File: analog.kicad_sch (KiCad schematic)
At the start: 50 parts, among them J10 Spare diff in, J9 Sensor harness, U8 ADS1115 (0x48), U9 ADS1115 (0x49)

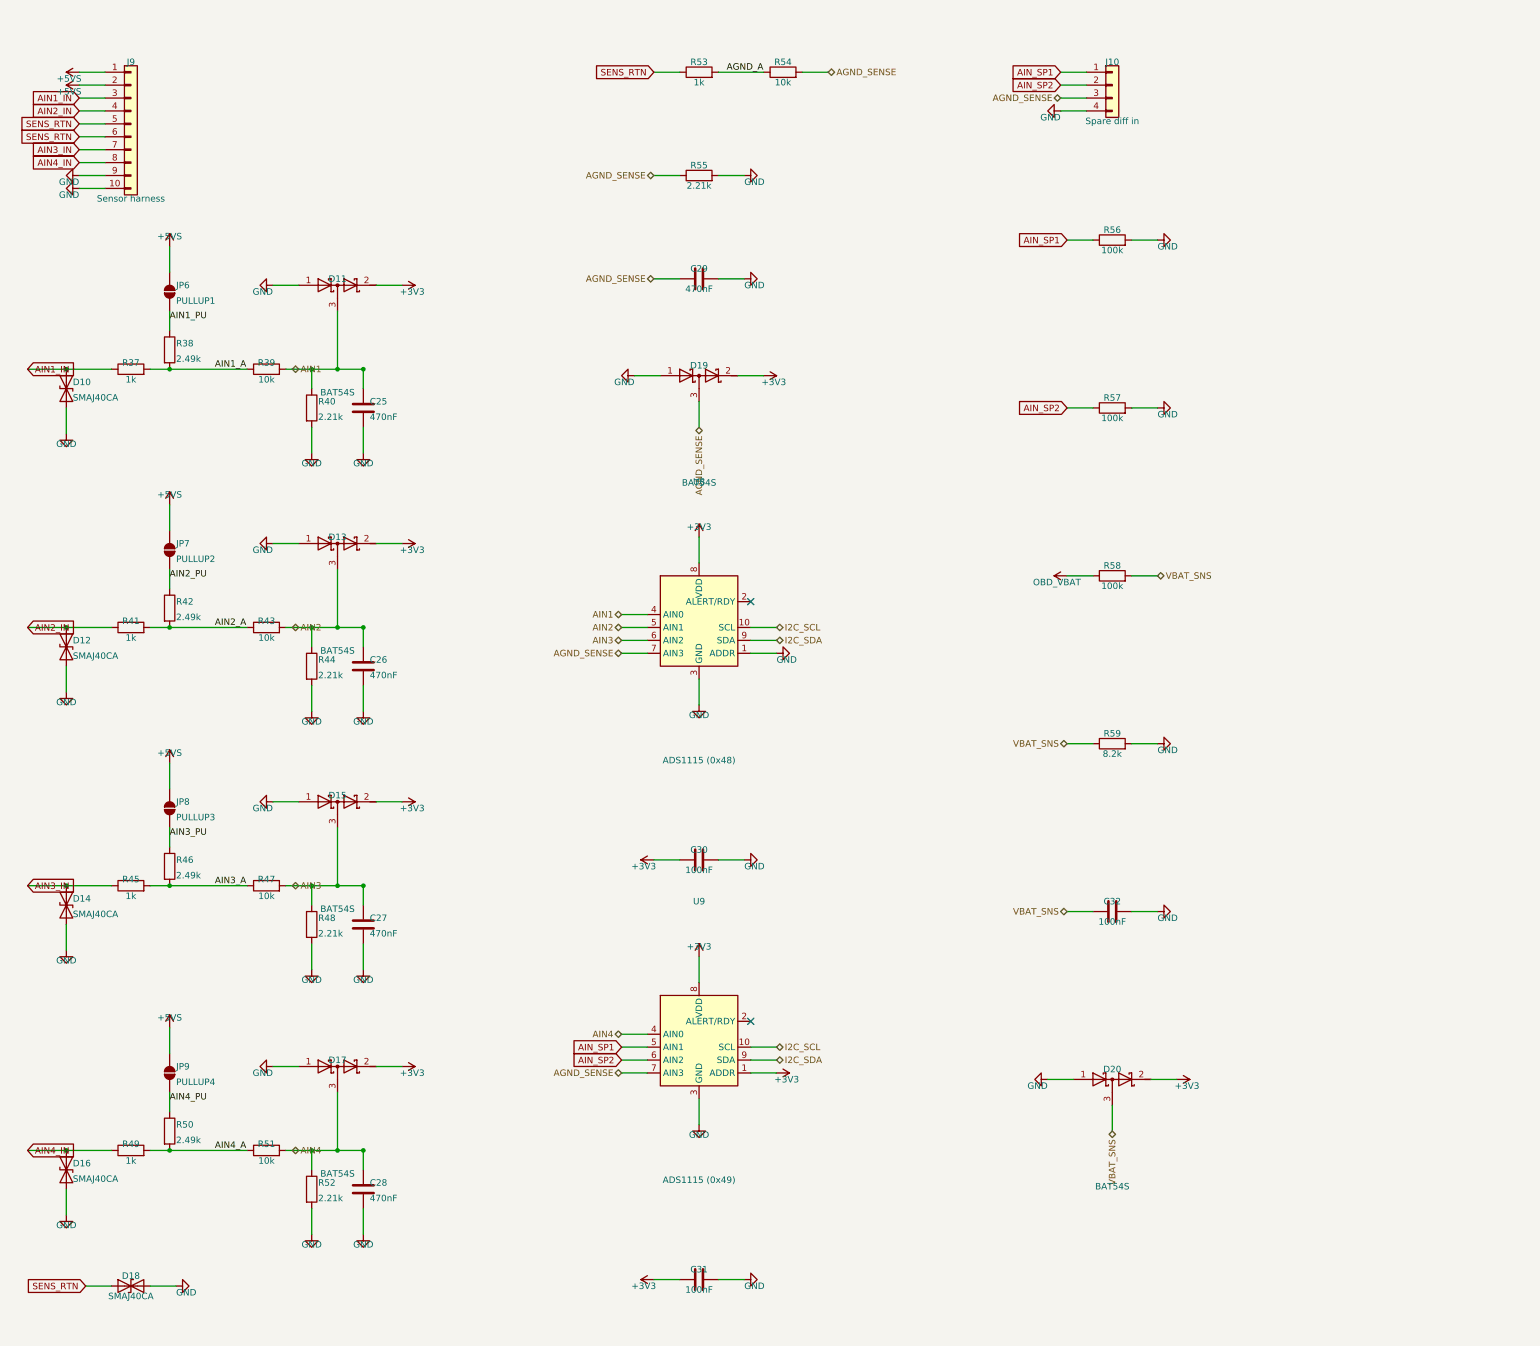
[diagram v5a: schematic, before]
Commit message: Make the schematic readable: wire the loose parts, stop text printing through symbols
Three things the drawing was doing badly, all now measured by a new
gen/audit_schematic.py rather than judged by eye.

LOOSE PARTS ARE WIRED NOW. A decoupling capacitor is a two-pin part with a
rail on each pin, and the column packer had no reason to put one next to
another -- so each came out as its own island with a net label at both ends,
twenty-odd of them down the edge of the power sheet. Electrically perfect,
visually a parts bin. build_ladders() groups the leftovers by which pair of
nets they sit across and draws each group as a proper ladder: one wire along
the top pins, one along the bottom, a junction at every rung and a power
symbol at each end. Nine groups across five sheets, including the supercap
bank and the battery monitor, and it removes two labels per part.

Grouping is on the actual pin GEOMETRY, not the symbol name, which is what
lets a balancing resistor share a ladder with the capacitor it balances while
keeping out a TVS diode whose pins are 1.3 mm closer together -- that one ERC
caught as two unconnected wire endpoints.

TEXT NO LONGER PRINTS THROUGH SYMBOLS. The offsets that place a reference and
a value work from the box around a part's PINS, and a symbol's graphic is
routinely drawn outside it. A power symbol's arrow therefore went straight
through its own name -- "+5VS" read "+2VS" at a glance, which is exactly how
somebody ends up probing the wrong rail -- and a capacitor lying on its side
has a y extent of exactly zero, so its reference and value printed across the
plates. Both now work from a floor on the body size. Rail names are also
centred on their own pin instead of drooping half a pitch onto the next one,
and the solder jumpers lost "(default OFF)" from their value into their note,
which is eighteen characters of text on a part 1.3 mm wide.

THE HAND-DRAWN BLOCKS WERE RE-SPACED to suit, because their tables were laid
out when the text sat closer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
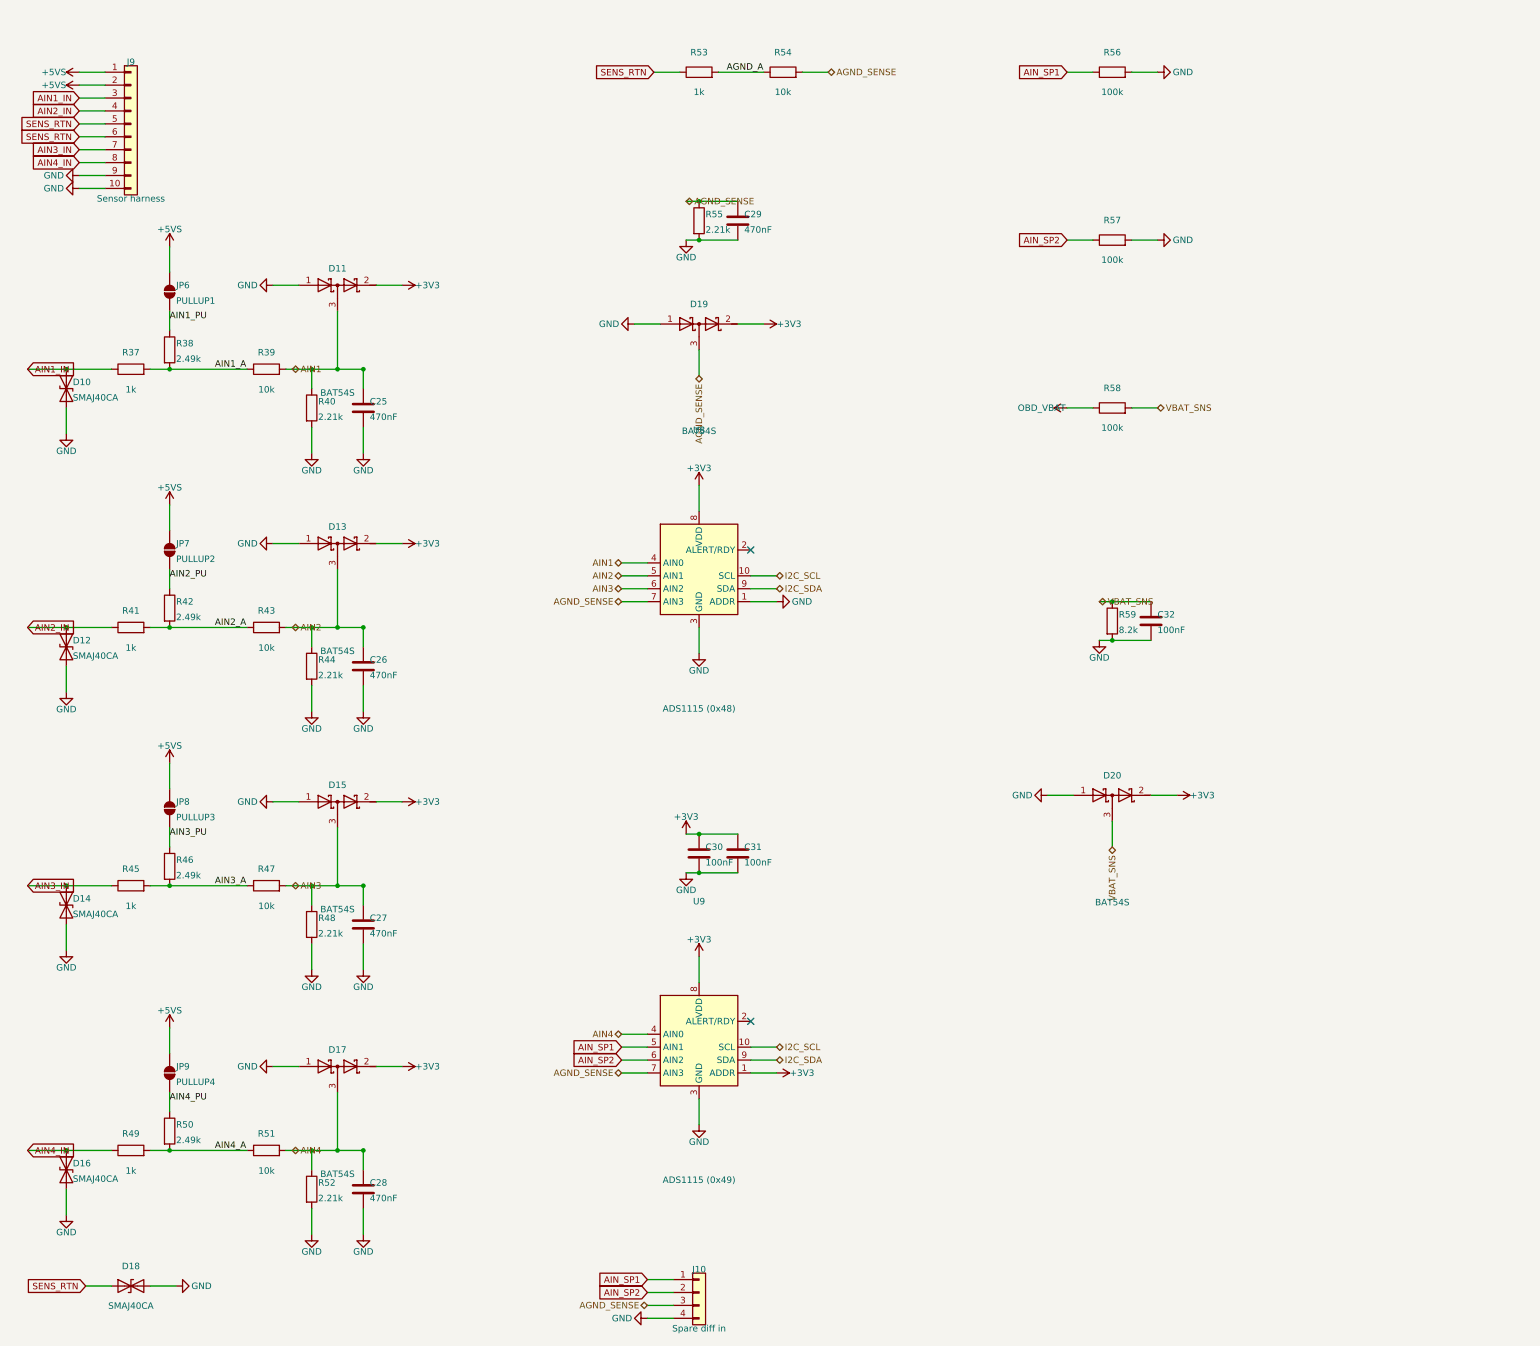
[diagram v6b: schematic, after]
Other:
- moved on the sheet: C29, C30, C31, C32, D19, D20, J10, R55, R56, R57, R58, R59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
